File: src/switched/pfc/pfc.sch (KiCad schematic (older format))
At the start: 68 parts, among them J1 AC-input, J2 Conn_01x02, J3 Conn_01x02, Q1 AOT190A60CL‎, U1 AP3917B, U2 bd7692fj

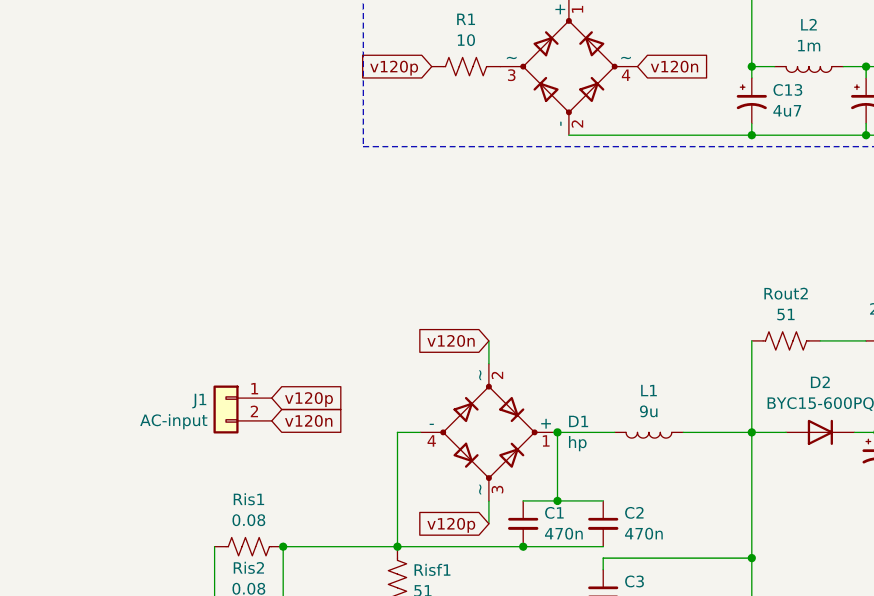
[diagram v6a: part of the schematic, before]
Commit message: Low effort input filter added to pfc, vestigial input port remains for potential issues
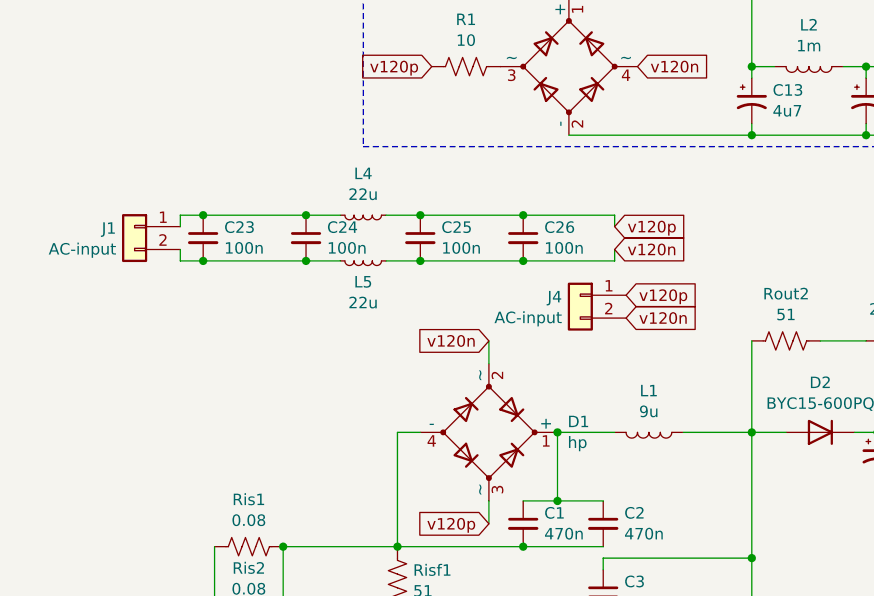
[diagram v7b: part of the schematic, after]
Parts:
- added C23, C24, C25, C26: 100n, Capacitor_SMD:C_1206_3216Metric_Pad1.33x1.80mm_HandSolder, symbol Device:C_Small
- added J4: AC-input, custom:spacedConnector, symbol Connector_Generic:Conn_01x02
- added L4, L5: 22u, custom:TMPC1206HP, symbol Device:L_Small
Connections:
- net v120n: now also C25.2, C26.2, J4.2 (Pin_2), L5.1; no longer J1.2 (Pin_2)
- net v120p: now also C25.1, C26.1, J4.1 (Pin_1), L4.1; no longer J1.1 (Pin_1)
- new net: C23.1, C24.1, J1.1 (Pin_1), L4.2
- new net: C23.2, C24.2, J1.2 (Pin_2), L5.2
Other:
- moved on the sheet: J1
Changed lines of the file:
@@
 Comment4 ""
 $EndDescr
-Text GLabel 1250 4250 2    50   Input ~ 0
+Text GLabel 2750 3500 2    50   Input ~ 0
 v120p
-Text GLabel 1250 4350 2    50   Input ~ 0
+Text GLabel 2750 3600 2    50   Input ~ 0
 v120n
 $Comp
@@
 L Connector_Generic:Conn_01x02 J1
 U 1 1 6023F774
-P 1050 4250
-F 0 "J1" H 1130 4242 50  0000 L CNN
-F 1 "AC-input" H 1130 4151 50  0000 L CNN
-F 2 "custom:spacedConnector" H 1050 4250 50  0001 C CNN
-F 3 "NA" H 1050 4250 50  0001 C CNN
-F 4 "0" H 1050 4250 50  0001 C CNN "price"
-F 5 "NA" H 1050 4250 50  0001 C CNN "Checked"
-F 6 "NA" H 1050 4250 50  0001 C CNN "Link"
-	1    1050 4250
+P 650 3500
+F 0 "J1" H 730 3492 50  0000 L CNN
+F 1 "AC-input" H 730 3401 50  0000 L CNN
+F 2 "custom:spacedConnector" H 650 3500 50  0001 C CNN
+F 3 "NA" H 650 3500 50  0001 C CNN
+F 4 "0" H 650 3500 50  0001 C CNN "price"
+F 5 "NA" H 650 3500 50  0001 C CNN "Checked"
+F 6 "NA" H 650 3500 50  0001 C CNN "Link"
+	1    650  3500
 	-1   0    0    -1
 $EndComp
@@
 Wire Wire Line
 	4000 5700 4350 5700
+$Comp
+L Device:L_Small L4
+U 1 1 604B54F3
+P 1650 3450
+F 0 "L4" V 1469 3450 50  0000 C CNN
+F 1 "22u" V 1560 3450 50  0000 C CNN
+F 2 "custom:TMPC1206HP" H 1650 3450 50  0001 C CNN
+F 3 "TMPC1206HP-220MG-D" H 1650 3450 50  0001 C CNN
+F 4 "https://lcsc.com/product-detail/Power-Inductors_TAI-TECH-TMPC1206HP-220MG-D_C357261.html" H 1650 3450 50  0001 C CNN "Link"
+	1    1650 3450
+	0    1    1    0
+$EndComp
+$Comp
+L Device:L_Small L5
+U 1 1 604B7224
+P 1650 3650
+F 0 "L5" V 1743 3650 50  0000 C CNN
+F 1 "22u" V 1834 3650 50  0000 C CNN
+F 2 "custom:TMPC1206HP" H 1650 3650 50  0001 C CNN
+F 3 "TMPC1206HP-220MG-D" H 1650 3650 50  0001 C CNN
+F 4 "https://lcsc.com/product-detail/Power-Inductors_TAI-TECH-TMPC1206HP-220MG-D_C357261.html" H 1650 3650 50  0001 C CNN "Link"
+	1    1650 3650
+	0    1    1    0
+$EndComp
+$Comp
+L Device:C_Small C25
+U 1 1 604C6D8F
+P 1900 3550
+F 0 "C25" H 1992 3596 50  0000 L CNN
+F 1 "100n" H 1992 3505 50  0000 L CNN
+F 2 "Capacitor_SMD:C_1206_3216Metric_Pad1.33x1.80mm_HandSolder" H 1900 3550 50  0001 C CNN
+F 3 "NM1206B104K451CEGN" H 1900 3550 50  0001 C CNN
+F 4 "https://lcsc.com/product-detail/Multilayer-Ceramic-Capacitors-MLCC-SMD-SMT_HUI-JU-NM1206B104K451CEGN_C710468.html" H 1900 3550 50  0001 C CNN "Link"
+F 5 "450" H 1900 3550 50  0001 C CNN "Working voltage"
+	1    1900 3550
+	1    0    0    -1
+$EndComp
+Wire Wire Line
+	1750 3650 1900 3650
+Wire Wire Line
+	1550 3650 1400 3650
+Wire Wire Line
+	1400 3450 1550 3450
+Wire Wire Line
+	1750 3450 1900 3450
+$Comp
+L Device:C_Small C24
+U 1 1 60504748
+P 1400 3550
+F 0 "C24" H 1492 3596 50  0000 L CNN
+F 1 "100n" H 1492 3505 50  0000 L CNN
+F 2 "Capacitor_SMD:C_1206_3216Metric_Pad1.33x1.80mm_HandSolder" H 1400 3550 50  0001 C CNN
+F 3 "NM1206B104K451CEGN" H 1400 3550 50  0001 C CNN
+F 4 "https://lcsc.com/product-detail/Multilayer-Ceramic-Capacitors-MLCC-SMD-SMT_HUI-JU-NM1206B104K451CEGN_C710468.html" H 1400 3550 50  0001 C CNN "Link"
+F 5 "450" H 1400 3550 50  0001 C CNN "Working voltage"
+	1    1400 3550
+	1    0    0    -1
+$EndComp
+$Comp
+L Device:C_Small C26
+U 1 1 60537560
+P 2350 3550
+F 0 "C26" H 2442 3596 50  0000 L CNN
+F 1 "100n" H 2442 3505 50  0000 L CNN
+F 2 "Capacitor_SMD:C_1206_3216Metric_Pad1.33x1.80mm_HandSolder" H 2350 3550 50  0001 C CNN
+F 3 "NM1206B104K451CEGN" H 2350 3550 50  0001 C CNN
+F 4 "https://lcsc.com/product-detail/Multilayer-Ceramic-Capacitors-MLCC-SMD-SMT_HUI-JU-NM1206B104K451CEGN_C710468.html" H 2350 3550 50  0001 C CNN "Link"
+F 5 "450" H 2350 3550 50  0001 C CNN "Working voltage"
+	1    2350 3550
+	1    0    0    -1
+$EndComp
+$Comp
+L Device:C_Small C23
+U 1 1 6053FE58
+P 950 3550
+F 0 "C23" H 1042 3596 50  0000 L CNN
+F 1 "100n" H 1042 3505 50  0000 L CNN
+F 2 "Capacitor_SMD:C_1206_3216Metric_Pad1.33x1.80mm_HandSolder" H 950 3550 50  0001 C CNN
+F 3 "NM1206B104K451CEGN" H 950 3550 50  0001 C CNN
+F 4 "https://lcsc.com/product-detail/Multilayer-Ceramic-Capacitors-MLCC-SMD-SMT_HUI-JU-NM1206B104K451CEGN_C710468.html" H 950 3550 50  0001 C CNN "Link"
+F 5 "450" H 950 3550 50  0001 C CNN "Working voltage"
+	1    950  3550
+	1    0    0    -1
+$EndComp
+Connection ~ 1900 3650
+Wire Wire Line
+	2350 3450 1900 3450
+Connection ~ 1900 3450
+Wire Wire Line
+	950  3450 1400 3450
+Connection ~ 1400 3450
+Wire Wire Line
+	950  3650 1400 3650
+Connection ~ 1400 3650
+Wire Wire Line
+	850  3500 850  3450
+Wire Wire Line
+	850  3450 950  3450
+Connection ~ 950  3450
+Wire Wire Line
+	850  3600 850  3650
+Wire Wire Line
+	850  3650 950  3650
+Connection ~ 950  3650
+Wire Wire Line
+	2750 3600 2750 3650
+Wire Wire Line
+	1900 3650 2350 3650
+Connection ~ 2350 3650
+Wire Wire Line
+	2350 3650 2750 3650
+Wire Wire Line
+	2350 3450 2750 3450
+Wire Wire Line
+	2750 3450 2750 3500
+Connection ~ 2350 3450
+$Comp
+L Connector_Generic:Conn_01x02 J4
+U 1 1 6060490C
+P 2600 3800
+F 0 "J4" H 2680 3792 50  0000 L CNN
+F 1 "AC-input" H 2680 3701 50  0000 L CNN
+F 2 "custom:spacedConnector" H 2600 3800 50  0001 C CNN
+F 3 "NA" H 2600 3800 50  0001 C CNN
+F 4 "0" H 2600 3800 50  0001 C CNN "price"
+F 5 "NA" H 2600 3800 50  0001 C CNN "Checked"
+F 6 "NA" H 2600 3800 50  0001 C CNN "Link"
+	1    2600 3800
+	-1   0    0    -1
+$EndComp
+Text GLabel 2800 3800 2    50   Input ~ 0
+v120p
+Text GLabel 2800 3900 2    50   Input ~ 0
+v120n
 $EndSCHEMATC

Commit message: final boards and initial blinky
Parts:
- C1, C11, C2: Checked (none) -> yes; Link https://lcsc.com/product-detail/Multilayer-Ceramic-Capacitors-MLCC-SMD-SMT_PSA-Prosperity-Dielectrics-FM43X474K501EGG_C692318.html -> https://lcsc.com/product-detail/Multilayer-Ceramic-Capacitors-MLCC-SMD-SMT_IHHEC-HOLY-STONE-ENTERPRISE-CO-LTD-C1812X474K451T_C106175.html; Working voltage 500 -> 450
- C10, C12, C13, C14, C22, C23, C24, C25, C26, C4, C5, C7, C8, C9, Ceo2, Cisf1, D1, D2, D3, D4, D5, D6, L2, L3, L4, L5, R1, R10, R11, R2, R5, R6, R7, R8, R9, Rgs1, Ris1, Ris2, Ris3, Risf1, Risf2, Rout1, Rout2, Rovph1, Rovph2, Rovpl1, Rvsh1, Rvsh2, Rvsl1, Rvsl2: Checked (none) -> yes
- C15, C16, C17, C18, C21, Ceo1: Checked (none) -> yes; Link https://lcsc.com/search?q=CL10B474KA8NNNC -> https://lcsc.com/product-detail/Multilayer-Ceramic-Capacito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
- C19, C20, C3, C6: Checked (none) -> yes; Link https://lcsc.com/product-detail/Multilayer-Ceramic-Capacitors-MLCC-SMD-SMT_IHHEC-HOLY-STONE-ENTERPRISE-CO-LTD-C1206X221M102T_C961523.html -> https://lcsc.com/product-detail/Multilayer-Ceramic-Capacitors-MLCC-SMD-SMT_HUI-JU-NV1206B221K102CEDN_C710472.html
- R3, R4: Checked (none) -> yes; Link https://lcsc.com/product-detail/Metal-Film-Resistor-TH_5-6K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 -> https://lcsc.com/product-detail/Metal-Film-Resistor-TH_Huax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
- Reo1, Rt1: Checked (none) -> yes; Link https://lcsc.com/product-detail/High-Precision-Low-TCR-SMD-Resistors_UNI-ROYAL-Uniroyal-Elec-TC0350D3902T5H_C517681.html -> https://lcsc.com/product-detail/High-Precision-Low-TCR-SMD-Resistors_UNI-ROYAL-Uniroyal-Elec-TC0350B3902T5H_C517479.html
